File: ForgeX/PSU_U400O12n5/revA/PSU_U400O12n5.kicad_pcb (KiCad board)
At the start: 2 copper layers, 0 parts

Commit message: hbm_U40010 sot-363 package updates
, better handsoldering
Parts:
- added D1: SS36, Diode_SMD:D_SMA, F.Cu at (141.0, 111.2)
- added D2: SS14, Diode_SMD:D_SMA, F.Cu at (141.0, 115.8)
- added D3: BYV26EGP-E3/73, EasyEDA:DO-15_BD3.1-L6.7-P10.70-D0.9-FD, F.Cu at (135.6, 91.9)
- added H1: MountingHole, MountingHole:MountingHole_3.2mm_M3_DIN965, F.Cu at (123.5, 119.8)
- added H2: MountingHole, MountingHole:MountingHole_3.2mm_M3_DIN965, F.Cu at (167.3, 119.1)
- added J1: Screw_Terminal_01x03, Libmain:SPACER_M3_PCONN_2x03, F.Cu at (144.7, 60.6)
- added Q1: STD2HNK60Z, EasyEDA:TO-252-2_L6.6-W6.1-P4.57-LS9.9-BR, F.Cu at (148.2, 95.5)
- added U1: OB2263MP, EasyEDA:SOT-23-6_L2.9-W1.6-P0.95-LS2.8-BR, F.Cu at (151.0, 119.0)
- added U2: TL431DBZ, Package_TO_SOT_SMD:SOT-23, F.Cu at (147.5, 111.2)

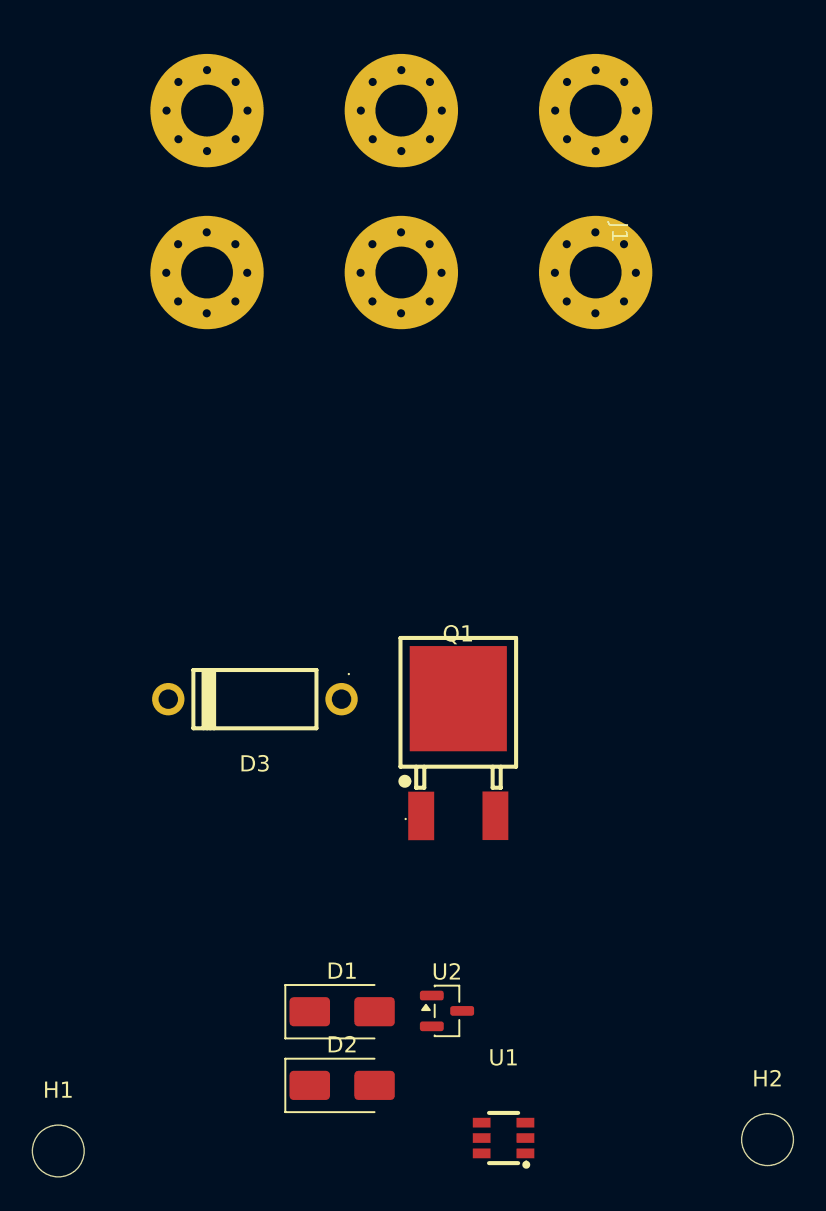
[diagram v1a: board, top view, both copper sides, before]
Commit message: Major redesign & Reworks
* Star grounding scheme enforced across the whole ForgeX design....
* Viper26 based PSU designed
* Better signal integrity & decoupling on LVP and major reroute
* Laminated DC bus (Biplanar) , instead of (Coplanar) , for heavily reduced bus inductance & equivelant Electrolytics ESL
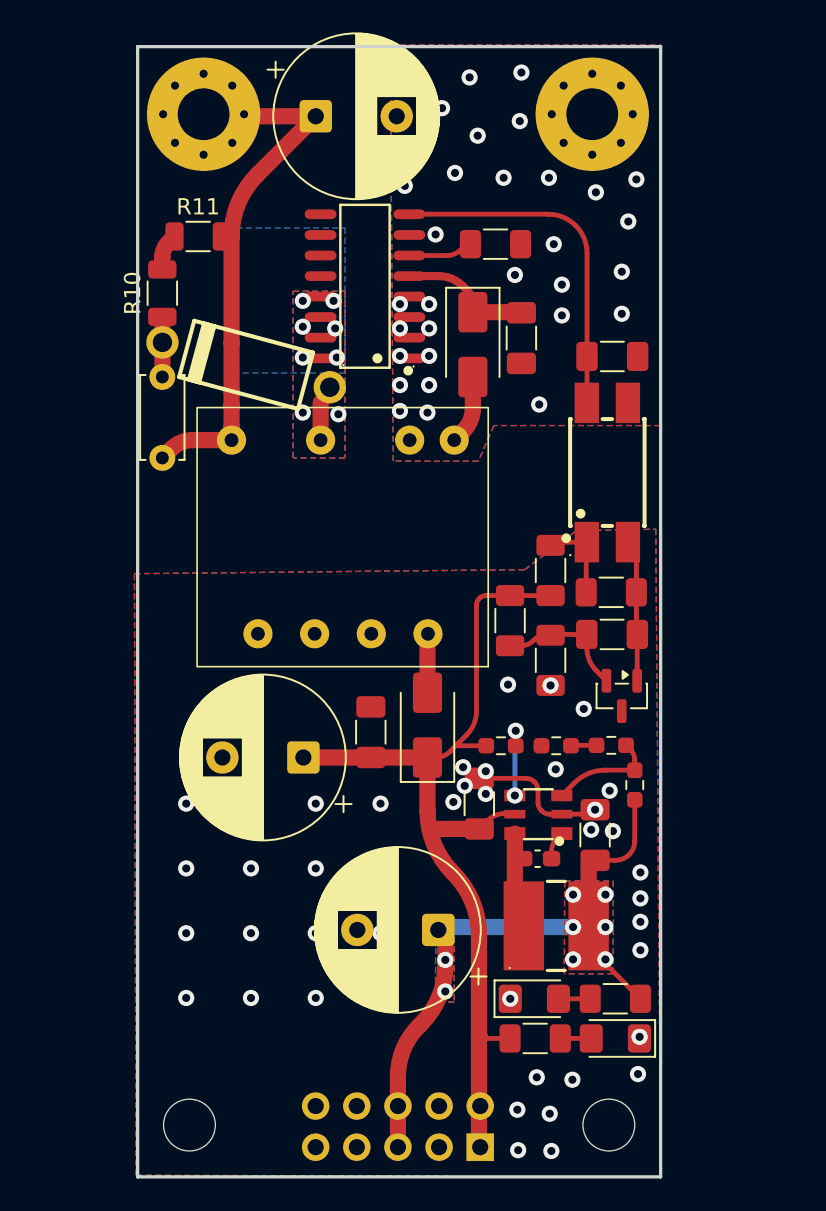
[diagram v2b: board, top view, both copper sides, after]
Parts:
- removed Q1: STD2HNK60Z, EasyEDA:TO-252-2_L6.6-W6.1-P4.57-LS9.9-BR
- added C1: 10u, Capacitor_SMD:C_1206_3216Metric_Pad1.33x1.80mm_HandSolder, F.Cu at (142.8, 93.9)
- added C10: 22u, Capacitor_SMD:C_1206_3216Metric_Pad1.33x1.80mm_HandSolder, F.Cu at (149.5, 98.4)
- added C11: 220u, Capacitor_THT:CP_Radial_D10.0mm_P5.00mm, F.Cu at (147.0, 106.2)
- added C2: 100p, Capacitor_SMD:C_1206_3216Metric_Pad1.33x1.80mm_HandSolder, F.Cu at (157.7, 87.9)
- added C3: 100n, Capacitor_SMD:C_1206_3216Metric_Pad1.33x1.80mm_HandSolder, F.Cu at (152.1, 69.6)
- added C4: 470u, Capacitor_THT:CP_Radial_D10.0mm_P5.00mm, F.Cu at (138.6, 95.5)
- added C5: 470p, Capacitor_THT:C_Disc_D5.0mm_W2.5mm_P5.00mm, F.Cu at (129.9, 77.0)
- added C6: 100p, Capacitor_SMD:C_1206_3216Metric_Pad1.33x1.80mm_HandSolder, F.Cu at (157.7, 70.7)
- added C7: C_Polarized, Capacitor_THT:CP_Radial_D10.0mm_P5.00mm, F.Cu at (139.4, 55.9)
- added C8: 22n, Capacitor_SMD:C_0603_1608Metric_Pad1.08x0.95mm_HandSolder, F.Cu at (153.1, 101.8)
- added C9: 22u, Capacitor_SMD:C_1206_3216Metric_Pad1.33x1.80mm_HandSolder, F.Cu at (156.7, 100.3)
- added D4: LED, LED_SMD:LED_1206_3216Metric_Pad1.42x1.75mm_HandSolder, F.Cu at (152.9, 110.4)
- added D5: LED, LED_SMD:LED_1206_3216Metric_Pad1.42x1.75mm_HandSolder, F.Cu at (157.9, 112.9)
- added J2: Conn_02x05_Odd_Even, Connector_PinHeader_2.54mm:PinHeader_2x05_P2.54mm_Vertical, B.Cu at (149.6, 119.6)
- added L2: CD54-150M_C49230812, EasyEDA:IND-SMD_L5.8-W5.2_CD54, F.Cu at (154.3, 105.9)
- added R1: 1k, Resistor_SMD:R_1206_3216Metric_Pad1.30x1.75mm_HandSolder, F.Cu at (157.9, 110.4)
- added R10: 10k, Resistor_SMD:R_1206_3216Metric, F.Cu at (129.9, 66.8)
- added R11: 10k, Resistor_SMD:R_1206_3216Metric, F.Cu at (132.1, 63.3)
- added R12: 1k, Resistor_SMD:R_1206_3216Metric_Pad1.30x1.75mm_HandSolder, F.Cu at (157.7, 85.3)
- added R13: 20k, Resistor_SMD:R_1206_3216Metric_Pad1.30x1.75mm_HandSolder, F.Cu at (150.5, 63.8)
- added R14: 6.8k, Resistor_SMD:R_0603_1608Metric_Pad0.98x0.95mm_HandSolder, F.Cu at (157.7, 94.8)
- added R15: 100k, Resistor_SMD:R_0603_1608Metric_Pad0.98x0.95mm_HandSolder, F.Cu at (159.1, 97.2)
- added R16: 6.8k, Resistor_SMD:R_0603_1608Metric_Pad0.98x0.95mm_HandSolder, F.Cu at (154.3, 94.8)
- added R17: 10k, Resistor_SMD:R_0603_1608Metric_Pad0.98x0.95mm_HandSolder, F.Cu at (150.8, 94.8)
- added R2: 5k, Resistor_SMD:R_1206_3216Metric_Pad1.30x1.75mm_HandSolder, F.Cu at (153.0, 112.9)
- added R7: 1k, Resistor_SMD:R_1206_3216Metric_Pad1.30x1.75mm_HandSolder, F.Cu at (153.9, 84.0)
- added R8: 1k, Resistor_SMD:R_1206_3216Metric_Pad1.30x1.75mm_HandSolder, F.Cu at (151.4, 87.1)
- added R9: 1k, Resistor_SMD:R_1206_3216Metric_Pad1.30x1.75mm_HandSolder, F.Cu at (153.9, 89.5)
- added U3: ~, Libmain:E16 Trans, F.Cu at (141.1, 81.9)
- added U4: PC817SC_C20612450, EasyEDA:OPTO-SMD-4_L4.6-W6.5-P2.54-LS10.3-TL, F.Cu at (157.4, 77.9)
- added U5: MT2492, EasyEDA:SOT-23-6_L2.9-W1.6-P0.95-LS2.8-BL_3, F.Cu at (153.1, 99.0)
- J1: value Screw_Terminal_01x03 -> Screw_Terminal_01x02; footprint Libmain:SPACER_M3_PCONN_2x03 -> Libmain:SPACER_M3_PCONN_PSU
- U1: value OB2263MP -> VIPER26LDTR; footprint EasyEDA:SOT-23-6_L2.9-W1.6-P0.95-LS2.8-BR -> EasyEDA:SOIC-16_L9.9-W3.9-P1.27-LS6.0-BL
- moved U1 53.3 mm to (142.4, 66.4), turned to 90 degrees
- moved D2 46.5 mm to (149.1, 70.0), turned to -90 degrees
- moved U2 22.2 mm to (158.3, 91.7), turned to -90 degrees
- moved D3 20.7 mm to (135.1, 71.3), turned to 165 degrees
- moved D1 18.5 mm to (146.3, 93.5), turned to 90 degrees
- moved H2 9.84 mm to (157.5, 118.2)
- moved H1 8.26 mm to (131.6, 118.2)
- moved J1 4.56 mm to (144.5, 56.0)
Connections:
- D1 pad 1: /12V -> +12V
- J1 pad 2: unconnected-(J1-Pin_2-Pad2)_14 -> GNDPWR
- U1 pad 1: GND -> GNDPWR
- U1 pad 2: unconnected-(U1-FB-Pad2) -> GNDPWR
- U1 pad 3: Net-(U1-RI) -> GNDPWR
- U1 pad 4: Net-(Q1-S) -> GNDPWR
- U1 pad 5: Net-(U1-VDD) -> /Aux
- U2 pad 1: /12V -> Net-(U2-K)
- U2 pad 2: unconnected-(U2-REF-Pad2) -> Net-(U2-REF)
- U2 pad 3: GND1 -> GND
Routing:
- net +12V: track 0.00 -> 57.5 mm
- net /VDCH: track 0.00 -> 40.2 mm
- net +5V: track 0.00 -> 35.0 mm, vias 0 -> 8
- net /FB: track 0.00 -> 21.6 mm
- net GND: track 0.00 -> 8.81 mm, vias 0 -> 42
- net Net-(U2-K): track 0.00 -> 8.76 mm
- net /Aux: track 0.00 -> 8.05 mm
- net Net-(U2-REF): track 0.00 -> 7.79 mm
- net Net-(U5-FB): track 0.00 -> 6.74 mm
- net Net-(U4-AN): track 0.00 -> 5.39 mm
- net Net-(U5-SW): track 0.00 -> 4.75 mm
- net Net-(D2-A): track 0.00 -> 4.28 mm
- net Net-(U5-EN): track 0.00 -> 4.02 mm, vias 0 -> 2
- net Net-(U1-LIM): track 0.00 -> 3.99 mm
- net Net-(D3-C): track 0.00 -> 3.72 mm
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- added copper zone on B.Cu, net +5V
- added copper zone on F.Cu, net +5V
- added copper zone on B.Cu, net GND
- added copper zone on F.Cu, net GND
- added copper zone on B.Cu, net GNDPWR
- added copper zone on F.Cu, net GNDPWR
- added copper zone on B.Cu, net Net-(D3-A)
- added copper zone on F.Cu, net Net-(D3-A)
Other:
- board outline added: 32.3 x 69.8 mm
